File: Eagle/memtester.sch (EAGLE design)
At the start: 15 parts, among them IC1 HT7833, J3 SM08B-SRSS-TB(LF)(SN), U1 ATTINY1616-MFR

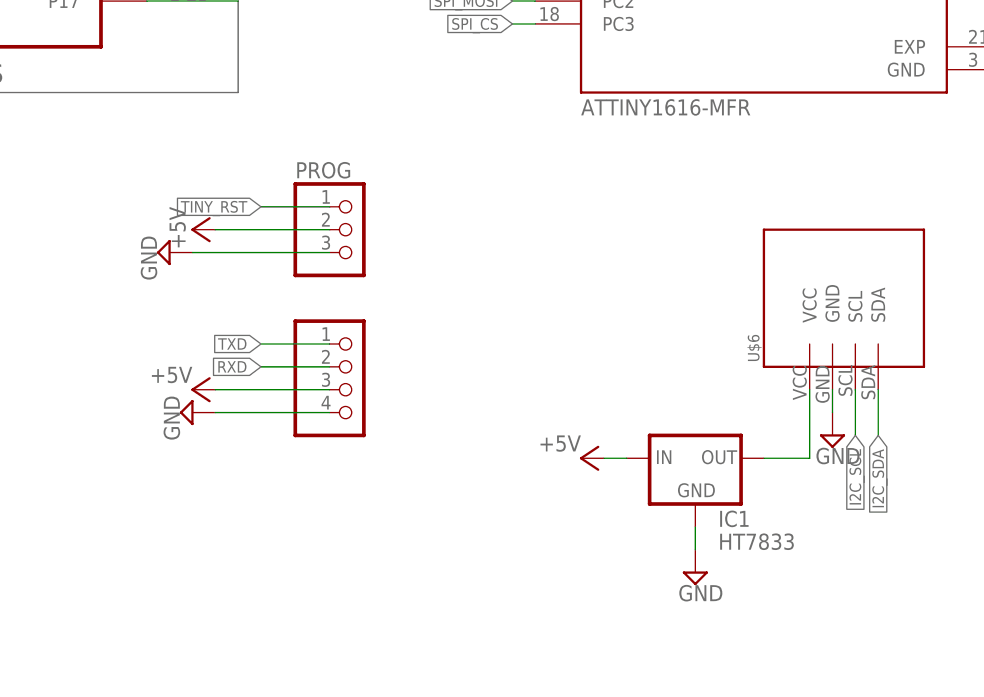
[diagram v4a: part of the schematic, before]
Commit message: Memtester: i2c pull-ups, labels, credits
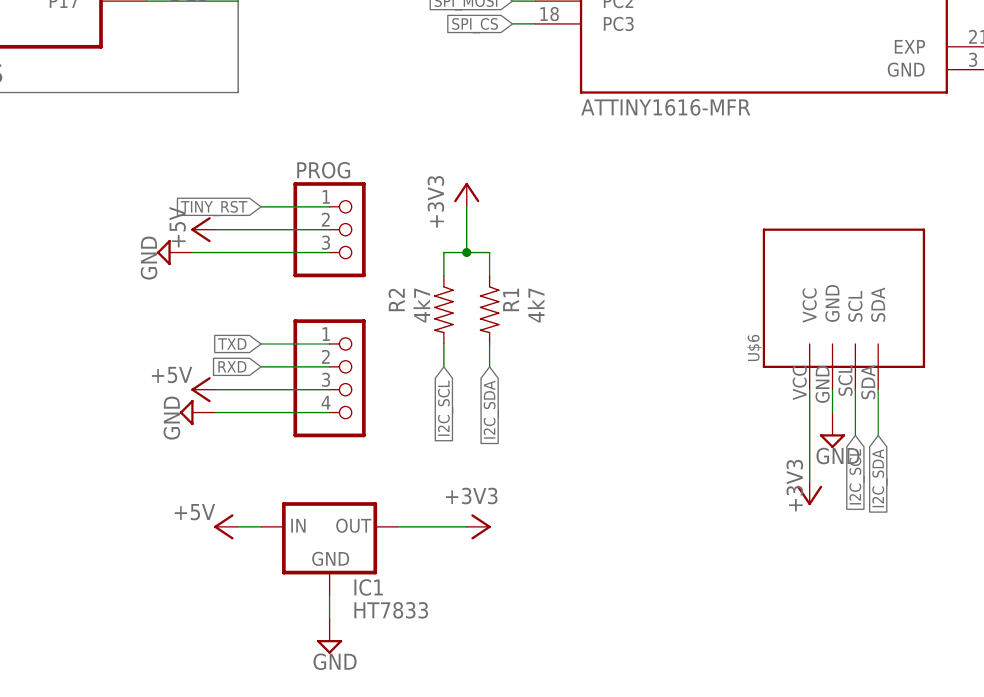
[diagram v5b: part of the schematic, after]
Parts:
- added R1, R2: 4k7, passives:RESISTOR0402_RES
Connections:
- removed net N$1: IC1.OUT, U$6.VCC
- new net +3V3: IC1.OUT, R1.1, R2.1, U$6.VCC
- net I2C_SCL: now also R2.2
- net I2C_SDA: now also R1.2
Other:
- moved on the sheet: IC1
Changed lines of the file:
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@@
 <part name="P+11" library="supply1" library_urn="urn:adsk.eagle:library:371" deviceset="+5V" device=""/>
 <part name="C4" library="passives" deviceset="CAPACITOR" device="0402_CAP" value="100nF"/>
+<part name="R2" library="passives" deviceset="RESISTOR" device="0402_RES" value="4k7"/>
+<part name="R1" library="passives" deviceset="RESISTOR" device="0402_RES" value="4k7"/>
+<part name="+3V12" library="supply1" library_urn="urn:adsk.eagle:library:371" deviceset="+3V3" device=""/>
+<part name="+3V1" library="supply1" library_urn="urn:adsk.eagle:library:371" deviceset="+3V3" device=""/>
+<part name="+3V2" library="supply1" library_urn="urn:adsk.eagle:library:371" deviceset="+3V3" device=""/>
 </parts>
 <sheets>
@@
 <attribute name="VALUE" x="182.88" y="0" size="1.778" layer="96" rot="R90"/>
 </instance>
-<instance part="IC1" gate="G$1" x="127" y="-25.4" smashed="yes">
-<attribute name="NAME" x="129.54" y="-33.02" size="1.778" layer="95"/>
-<attribute name="VALUE" x="129.54" y="-35.56" size="1.778" layer="96"/>
-<attribute name="LCSC_PART" x="127" y="-25.4" size="1.27" layer="96" display="off"/>
+<instance part="IC1" gate="G$1" x="86.36" y="-33.02" smashed="yes">
+<attribute name="NAME" x="88.9" y="-40.64" size="1.778" layer="95"/>
+<attribute name="VALUE" x="88.9" y="-43.18" size="1.778" layer="96"/>
+<attribute name="LCSC_PART" x="86.36" y="-33.02" size="1.27" layer="96" display="off"/>
 </instance>
 <instance part="SUPPLY12" gate="GND" x="172.72" y="-5.08" smashed="yes" rot="R270">
 <attribute name="VALUE" x="169.545" y="-3.175" size="1.778" layer="96" rot="R270"/>
 </instance>
-<instance part="SUPPLY13" gate="GND" x="127" y="-38.1" smashed="yes">
-<attribute name="VALUE" x="125.095" y="-41.275" size="1.778" layer="96"/>
-</instance>
-<instance part="P+11" gate="1" x="114.3" y="-25.4" smashed="yes" rot="R90">
-<attribute name="VALUE" x="114.3" y="-22.86" size="1.778" layer="96" rot="R180"/>
+<instance part="SUPPLY13" gate="GND" x="86.36" y="-45.72" smashed="yes">
+<attribute name="VALUE" x="84.455" y="-48.895" size="1.778" layer="96"/>
+</instance>
+<instance part="P+11" gate="1" x="73.66" y="-33.02" smashed="yes" rot="R90">
+<attribute name="VALUE" x="73.66" y="-30.48" size="1.778" layer="96" rot="R180"/>
 </instance>
 <instance part="C4" gate="G$1" x="139.7" y="85.09" smashed="yes">
 <attribute name="NAME" x="141.224" y="85.471" size="1.778" layer="95"/>
 <attribute name="VALUE" x="141.224" y="80.391" size="1.778" layer="96"/>
+</instance>
+<instance part="R2" gate="G$1" x="99.06" y="-10.16" smashed="yes" rot="R270">
+<attribute name="NAME" x="92.9386" y="-6.35" size="1.778" layer="95" rot="R270"/>
+<attribute name="VALUE" x="95.758" y="-6.35" size="1.778" layer="96" rot="R270"/>
+</instance>
+<instance part="R1" gate="G$1" x="104.14" y="-10.16" smashed="yes" rot="R270">
+<attribute name="NAME" x="105.6386" y="-6.35" size="1.778" layer="95" rot="R270"/>
+<attribute name="VALUE" x="108.458" y="-6.35" size="1.778" layer="96" rot="R270"/>
+</instance>
+<instance part="+3V12" gate="G$1" x="101.6" y="5.08" smashed="yes">
+<attribute name="VALUE" x="99.06" y="0" size="1.778" layer="96" rot="R90"/>
+</instance>
+<instance part="+3V1" gate="G$1" x="104.14" y="-33.02" smashed="yes" rot="R270">
+<attribute name="VALUE" x="99.06" y="-30.48" size="1.778" layer="96"/>
+</instance>
+<instance part="+3V2" gate="G$1" x="139.7" y="-30.48" smashed="yes" rot="R180">
+<attribute name="VALUE" x="137.16" y="-25.4" size="1.778" layer="96" rot="R270"/>
 </instance>
 </instances>
@@
 <pinref part="P+11" gate="1" pin="+5V"/>
 <pinref part="IC1" gate="G$1" pin="IN"/>
-<wire x1="116.84" y1="-25.4" x2="119.38" y2="-25.4" width="0.1524" layer="91"/>
+<wire x1="76.2" y1="-33.02" x2="78.74" y2="-33.02" width="0.1524" layer="91"/>
 </segment>
 </net>
@@
 <pinref part="IC1" gate="G$1" pin="GND"/>
 <pinref part="SUPPLY13" gate="GND" pin="GND"/>
-<wire x1="127" y1="-33.02" x2="127" y2="-35.56" width="0.1524" layer="91"/>
+<wire x1="86.36" y1="-40.64" x2="86.36" y2="-43.18" width="0.1524" layer="91"/>
 </segment>
 </net>
@@
 <pinref part="J3" gate="G$2" pin="8"/>
 </segment>
+<segment>
+<wire x1="104.14" y1="-12.7" x2="104.14" y2="-15.24" width="0.1524" layer="91"/>
+<label x="104.14" y="-15.24" size="1.27" layer="95" rot="R270" xref="yes"/>
+<pinref part="R1" gate="G$1" pin="2"/>
+</segment>
 </net>
 <net name="I2C_SCL" class="0">
@@
 <pinref part="J3" gate="G$2" pin="7"/>
 </segment>
+<segment>
+<wire x1="99.06" y1="-12.7" x2="99.06" y2="-15.24" width="0.1524" layer="91"/>
+<label x="99.06" y="-15.24" size="1.27" layer="95" rot="R270" xref="yes"/>
+<pinref part="R2" gate="G$1" pin="2"/>
+</segment>
 </net>
 <net name="OE" class="0">
@@
 </segment>
 </net>
-<net name="N$1" class="0">
+<net name="+3V3" class="0">
+<segment>
+<pinref part="R2" gate="G$1" pin="1"/>
+<wire x1="99.06" y1="-5.08" x2="99.06" y2="-2.54" width="0.1524" layer="91"/>
+<wire x1="99.06" y1="-2.54" x2="101.6" y2="-2.54" width="0.1524" layer="91"/>
+<pinref part="R1" gate="G$1" pin="1"/>
+<wire x1="101.6" y1="-2.54" x2="104.14" y2="-2.54" width="0.1524" layer="91"/>
+<wire x1="104.14" y1="-2.54" x2="104.14" y2="-5.08" width="0.1524" layer="91"/>
+<pinref part="+3V12" gate="G$1" pin="+3V3"/>
+<wire x1="101.6" y1="2.54" x2="101.6" y2="-2.54" width="0.1524" layer="91"/>
+<junction x="101.6" y="-2.54"/>
+</segment>
 <segment>
 <pinref part="IC1" gate="G$1" pin="OUT"/>
+<pinref part="+3V1" gate="G$1" pin="+3V3"/>
+<wire x1="93.98" y1="-33.02" x2="101.6" y2="-33.02" width="0.1524" layer="91"/>
+</segment>
+<segment>
+<pinref part="+3V2" gate="G$1" pin="+3V3"/>
 <pinref part="U$6" gate="G$1" pin="VCC"/>
-<wire x1="134.62" y1="-25.4" x2="139.7" y2="-25.4" width="0.1524" layer="91"/>
-<wire x1="139.7" y1="-25.4" x2="139.7" y2="-17.78" width="0.1524" layer="91"/>
-</segment>
-</net>
+<wire x1="139.7" y1="-27.94" x2="139.7" y2="-17.78" width="0.1524" layer="91"/>
+</segment>
+</net>

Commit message: Memtester: leds, button
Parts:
- added LED1, LED2: green, led:LEDCHIP-LED0805
- added R3, R4: 2k, passives:RESISTOR0402_RES
- added SW1: BTN, SparkFun-Switches:MOMENTARY-SWITCH-SPST-SMD-6.0X3.5MM
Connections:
- new net N$2: LED1.C, R3.1
- new net N$3: LED2.C, R4.1
- net GND: now also R3.2, R4.2, SW1.2
- net PB2: now also SW1.1
- net PB4: now also LED1.A
- net PB5: now also LED2.A

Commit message: Memtester: Labels, wirestubs
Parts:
- added SW2: BTN, SparkFun-Switches:MOMENTARY-SWITCH-SPST-SMD-6.0X3.5MM
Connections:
- net GND: now also SW2.2
- net PB3: now also SW2.1
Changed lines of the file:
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@@
 <grid distance="0.1" unitdist="inch" unit="inch" style="lines" multiple="1" display="no" altdistance="0.01" altunitdist="inch" altunit="inch"/>
 <layers>
-<layer number="1" name="Top" color="4" fill="1" visible="yes" active="no"/>
-<layer number="2" name="Route2" color="16" fill="1" visible="yes" active="no"/>
-<layer number="15" name="Route15" color="23" fill="1" visible="yes" active="no"/>
-<layer number="16" name="Bottom" color="1" fill="1" visible="yes" active="no"/>
-<layer number="17" name="Pads" color="2" fill="1" visible="yes" active="no"/>
-<layer number="18" name="Vias" color="2" fill="1" visible="yes" active="no"/>
-<layer number="19" name="Unrouted" color="6" fill="1" visible="yes" active="no"/>
-<layer number="20" name="Dimension" color="24" fill="1" visible="yes" active="no"/>
-<layer number="21" name="tPlace" color="7" fill="1" visible="yes" active="no"/>
-<layer number="22" name="bPlace" color="7" fill="1" visible="yes" active="no"/>
-<layer number="23" name="tOrigins" color="15" fill="1" visible="yes" active="no"/>
-<layer number="24" name="bOrigins" color="15" fill="1" visible="yes" active="no"/>
-<layer number="25" name="tNames" color="7" fill="1" visible="yes" active="no"/>
-<layer number="26" name="bNames" color="7" fill="1" visible="yes" active="no"/>
-<layer number="27" name="tValues" color="7" fill="1" visible="yes" active="no"/>
-<layer number="28" name="bValues" color="7" fill="1" visible="yes" active="no"/>
+<layer number="1" name="Top" color="4" fill="1" visible="no" active="no"/>
+<layer number="2" name="Route2" color="16" fill="1" visible="no" active="no"/>
+<layer number="15" name="Route15" color="23" fill="1" visible="no" active="no"/>
+<layer number="16" name="Bottom" color="1" fill="1" visible="no" active="no"/>
+<layer number="17" name="Pads" color="2" fill="1" visible="no" active="no"/>
+<layer number="18" name="Vias" color="2" fill="1" visible="no" active="no"/>
+<layer number="19" name="Unrouted" color="6" fill="1" visible="no" active="no"/>
+<layer number="20" name="Dimension" color="24" fill="1" visible="no" active="no"/>
+<layer number="21" name="tPlace" color="7" fill="1" visible="no" active="no"/>
+<layer number="22" name="bPlace" color="7" fill="1" visible="no" active="no"/>
+<layer number="23" name="tOrigins" color="15" fill="1" visible="no" active="no"/>
+<layer number="24" name="bOrigins" color="15" fill="1" visible="no" active="no"/>
+<layer number="25" name="tNames" color="7" fill="1" visible="no" active="no"/>
+<layer number="26" name="bNames" color="7" fill="1" visible="no" active="no"/>
+<layer number="27" name="tValues" color="7" fill="1" visible="no" active="no"/>
+<layer number="28" name="bValues" color="7" fill="1" visible="no" active="no"/>
 <layer number="29" name="tStop" color="7" fill="3" visible="no" active="no"/>
 <layer number="30" name="bStop" color="7" fill="6" visible="no" active="no"/>
@@
 <layer number="35" name="tGlue" color="7" fill="4" visible="no" active="no"/>
 <layer number="36" name="bGlue" color="7" fill="5" visible="no" active="no"/>
-<layer number="37" name="tTest" color="7" fill="1" visible="yes" active="no"/>
-<layer number="38" name="bTest" color="7" fill="1" visible="yes" active="no"/>
+<layer number="37" name="tTest" color="7" fill="1" visible="no" active="no"/>
+<layer number="38" name="bTest" color="7" fill="1" visible="no" active="no"/>
 <layer number="39" name="tKeepout" color="4" fill="11" visible="no" active="no"/>
 <layer number="40" name="bKeepout" color="1" fill="11" visible="no" active="no"/>
@@
 <layer number="44" name="Drills" color="7" fill="1" visible="no" active="no"/>
 <layer number="45" name="Holes" color="7" fill="1" visible="no" active="no"/>
-<layer number="46" name="Milling" color="3" fill="1" visible="yes" active="no"/>
-<layer number="47" name="Measures" color="7" fill="1" visible="yes" active="no"/>
-<layer number="48" name="Document" color="7" fill="1" visible="yes" active="no"/>
-<layer number="49" name="Reference" color="7" fill="1" visible="yes" active="no"/>
-<layer number="50" name="dxf" color="7" fill="1" visible="yes" active="no"/>
-<layer number="51" name="tDocu" color="7" fill="1" visible="yes" active="no"/>
-<layer number="52" name="bDocu" color="7" fill="1" visible="yes" active="no"/>
-<layer number="53" name="tGND_GNDA" color="7" fill="1" visible="yes" active="no"/>
-<layer number="54" name="bGND_GNDA" color="7" fill="1" visible="yes" active="no"/>
-<layer number="56" name="wert" color="7" fill="1" visible="yes" active="no"/>
-<layer number="57" name="tCAD" color="7" fill="1" visible="yes" active="no"/>
-<layer number="58" name="bCAD" color="7" fill="1" visible="yes" active="no"/>
-<layer number="59" name="tCarbon" color="7" fill="1" visible="yes" active="no"/>
-<layer number="60" name="bCarbon" color="7" fill="1" visible="yes" active="no"/>
-<layer number="61" name="stand" color="7" fill="1" visible="yes" active="no"/>
+<layer number="46" name="Milling" color="3" fill="1" visible="no" active="no"/>
+<layer number="47" name="Measures" color="7" fill="1" visible="no" active="no"/>
+<layer number="48" name="Document" color="7" fill="1" visible="no" active="no"/>
+<layer number="49" name="Reference" color="7" fill="1" visible="no" active="no"/>
+<layer number="50" name="dxf" color="7" fill="1" visible="no" active="no"/>
+<layer number="51" name="tDocu" color="7" fill="1" visible="no" active="no"/>
+<layer number="52" name="bDocu" color="7" fill="1" visible="no" active="no"/>
+<layer number="53" name="tGND_GNDA" color="7" fill="1" visible="no" active="no"/>
+<layer number="54" name="bGND_GNDA" color="7" fill="1" visible="no" active="no"/>
+<layer number="56" name="wert" color="7" fill="1" visible="no" active="no"/>
+<layer number="57" name="tCAD" color="7" fill="1" visible="no" active="no"/>
+<layer number="58" name="bCAD" color="7" fill="1" visible="no" active="no"/>
+<layer number="59" name="tCarbon" color="7" fill="1" visible="no" active="no"/>
+<layer number="60" name="bCarbon" color="7" fill="1" visible="no" active="no"/>
+<layer number="61" name="stand" color="7" fill="1" visible="no" active="no"/>
 <layer number="88" name="SimResults" color="9" fill="1" visible="yes" active="yes"/>
 <layer number="89" name="SimProbes" color="9" fill="1" visible="yes" active="yes"/>
@@
 <attribute name="LCSC_PART" value="C118141"/>
 </part>
+<part name="SW2" library="SparkFun-Switches" deviceset="MOMENTARY-SWITCH-SPST" device="-SMD-6.0X3.5MM" value="BTN">
+<attribute name="LCSC_PART" value="C118141"/>
+</part>
 </parts>
 <sheets>
@@
 <attribute name="VALUE" x="15.748" y="-2.54" size="1.778" layer="96" font="vector" rot="R90" align="top-center"/>
 <attribute name="LCSC_PART" x="15.24" y="-2.54" size="1.778" layer="96" rot="R90" display="off"/>
+</instance>
+<instance part="SW2" gate="G$1" x="20.32" y="-2.54" smashed="yes" rot="R90">
+<attribute name="NAME" x="18.796" y="-2.54" size="1.778" layer="95" font="vector" rot="R90" align="bottom-center"/>
+<attribute name="VALUE" x="20.828" y="-2.54" size="1.778" layer="96" font="vector" rot="R90" align="top-center"/>
+<attribute name="LCSC_PART" x="20.32" y="-2.54" size="1.778" layer="96" rot="R90" display="off"/>
 </instance>
 </instances>
@@
 <wire x1="15.24" y1="7.62" x2="15.24" y2="2.54" width="0.1524" layer="91"/>
 <junction x="5.08" y="7.62"/>
+<pinref part="SW2" gate="G$1" pin="2"/>
+<wire x1="15.24" y1="7.62" x2="20.32" y2="7.62" width="0.1524" layer="91"/>
+<wire x1="20.32" y1="7.62" x2="20.32" y2="2.54" width="0.1524" layer="91"/>
+<junction x="15.24" y="7.62"/>
 </segment>
 </net>
@@
 <pinref part="U1" gate="G$1" pin="PB3/TOSC1"/>
 </segment>
-</net>
+<segment>
+<pinref part="SW2" gate="G$1" pin="1"/>
+<wire x1="20.32" y1="-7.62" x2="20.32" y2="-17.78" width="0.1524" layer="91"/>
+<label x="20.32" y="-17.78" size="1.27" layer="95" rot="R270" xref="yes"/>
+</segment>
+</net>

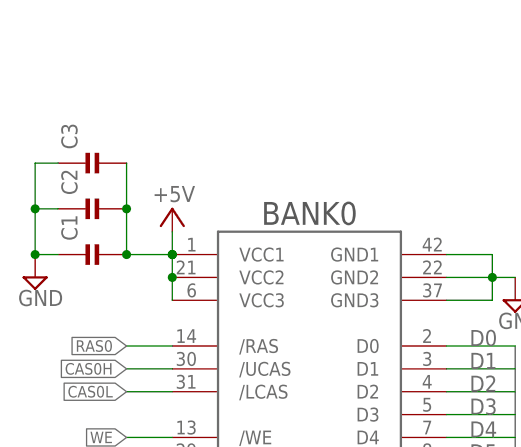
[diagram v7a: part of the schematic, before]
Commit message: Memtester: C values
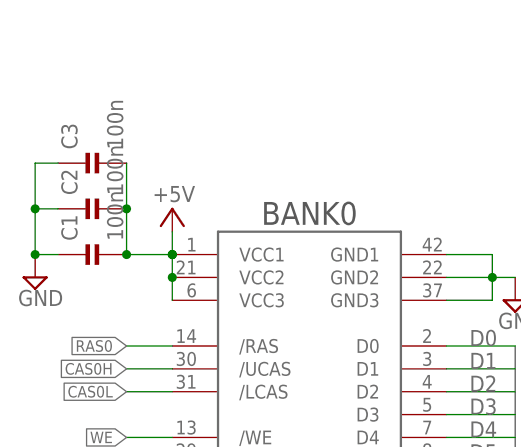
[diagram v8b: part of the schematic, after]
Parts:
- C1, C2, C3: value (none) -> 100n
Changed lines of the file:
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@@
 <parts>
 <part name="P+1" library="supply1" library_urn="urn:adsk.eagle:library:371" deviceset="+5V" device=""/>
-<part name="C1" library="passives" deviceset="CAPACITOR" device="0402_CAP"/>
-<part name="C2" library="passives" deviceset="CAPACITOR" device="0402_CAP"/>
-<part name="C3" library="passives" deviceset="CAPACITOR" device="0402_CAP"/>
+<part name="C1" library="passives" deviceset="CAPACITOR" device="0402_CAP" value="100n"/>
+<part name="C2" library="passives" deviceset="CAPACITOR" device="0402_CAP" value="100n"/>
+<part name="C3" library="passives" deviceset="CAPACITOR" device="0402_CAP" value="100n"/>
 <part name="SUPPLY1" library="supply2" library_urn="urn:adsk.eagle:library:372" deviceset="GND" device=""/>
 <part name="SUPPLY2" library="supply2" library_urn="urn:adsk.eagle:library:372" deviceset="GND" device=""/>
